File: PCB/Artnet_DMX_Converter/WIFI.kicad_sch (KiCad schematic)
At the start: 9 parts, among them J13 Conn_02x04

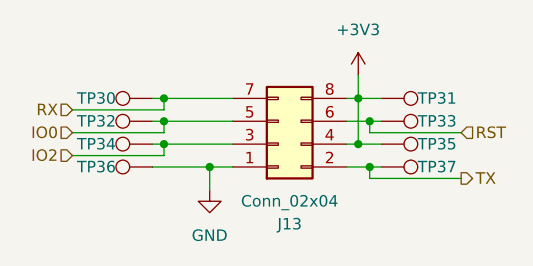
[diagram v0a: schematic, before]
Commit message: Testpoints and GND1 Fill
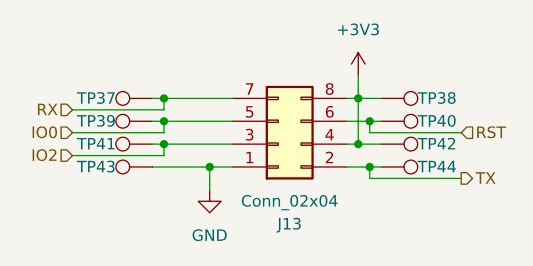
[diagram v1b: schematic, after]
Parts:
- renumbered TP30 to TP37, TP31 to TP38, TP32 to TP39, TP33 to TP40, TP34 to TP41, TP35 to TP42, TP36 to TP43, TP37 to TP44
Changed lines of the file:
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@@
 		(on_board yes)
 		(dnp no)
-		(property "Reference" "TP35"
+		(property "Reference" "TP42"
 			(at 155.194 87.63 90)
 			(effects
@@
 			(project "Artnet_DMX_Converter"
 				(path "/7d5b1976-98b3-4e47-ae52-3fe360235ea3/a6dafa22-90bf-43fa-b3bd-bb5c9d6a5370"
-					(reference "TP35")
+					(reference "TP42")
 					(unit 1)
 				)
@@
 		(dnp no)
 		(fields_autoplaced yes)
-		(property "Reference" "#PWR0135"
+		(property "Reference" "#PWR0140"
 			(at 148.59 83.82 0)
 			(effects
@@
 			(project ""
 				(path "/7d5b1976-98b3-4e47-ae52-3fe360235ea3/a6dafa22-90bf-43fa-b3bd-bb5c9d6a5370"
-					(reference "#PWR0135")
+					(reference "#PWR0140")
 					(unit 1)
 				)
@@
 		(on_board yes)
 		(dnp no)
-		(property "Reference" "TP30"
+		(property "Reference" "TP37"
 			(at 121.666 82.55 90)
 			(effects
@@
 			(project "Artnet_DMX_Converter"
 				(path "/7d5b1976-98b3-4e47-ae52-3fe360235ea3/a6dafa22-90bf-43fa-b3bd-bb5c9d6a5370"
-					(reference "TP30")
+					(reference "TP37")
 					(unit 1)
 				)
@@
 		(on_board yes)
 		(dnp no)
-		(property "Reference" "TP34"
+		(property "Reference" "TP41"
 			(at 121.666 87.63 90)
 			(effects
@@
 			(project "Artnet_DMX_Converter"
 				(path "/7d5b1976-98b3-4e47-ae52-3fe360235ea3/a6dafa22-90bf-43fa-b3bd-bb5c9d6a5370"
-					(reference "TP34")
+					(reference "TP41")
 					(unit 1)
 				)
@@
 		(dnp no)
 		(fields_autoplaced yes)
-		(property "Reference" "#PWR0136"
+		(property "Reference" "#PWR0141"
 			(at 132.08 99.06 0)
 			(effects
@@
 			(project ""
 				(path "/7d5b1976-98b3-4e47-ae52-3fe360235ea3/a6dafa22-90bf-43fa-b3bd-bb5c9d6a5370"
-					(reference "#PWR0136")
+					(reference "#PWR0141")
 					(unit 1)
 				)
@@
 		(on_board yes)
 		(dnp no)
-		(property "Reference" "TP36"
+		(property "Reference" "TP43"
 			(at 121.666 90.17 90)
 			(effects
@@
 			(project "Artnet_DMX_Converter"
 				(path "/7d5b1976-98b3-4e47-ae52-3fe360235ea3/a6dafa22-90bf-43fa-b3bd-bb5c9d6a5370"
-					(reference "TP36")
+					(reference "TP43")
 					(unit 1)
 				)
@@
 		(on_board yes)
 		(dnp no)
-		(property "Reference" "TP33"
+		(property "Reference" "TP40"
 			(at 155.194 85.09 90)
 			(effects
@@
 			(project "Artnet_DMX_Converter"
 				(path "/7d5b1976-98b3-4e47-ae52-3fe360235ea3/a6dafa22-90bf-43fa-b3bd-bb5c9d6a5370"
-					(reference "TP33")
+					(reference "TP40")
 					(unit 1)
 				)
@@
 		(on_board yes)
 		(dnp no)
-		(property "Reference" "TP32"
+		(property "Reference" "TP39"
 			(at 121.666 85.09 90)
 			(effects
@@
 			(project "Artnet_DMX_Converter"
 				(path "/7d5b1976-98b3-4e47-ae52-3fe360235ea3/a6dafa22-90bf-43fa-b3bd-bb5c9d6a5370"
-					(reference "TP32")
+					(reference "TP39")
 					(unit 1)
 				)
@@
 		(on_board yes)
 		(dnp no)
-		(property "Reference" "TP37"
+		(property "Reference" "TP44"
 			(at 155.194 90.17 90)
 			(effects
@@
 			(project "Artnet_DMX_Converter"
 				(path "/7d5b1976-98b3-4e47-ae52-3fe360235ea3/a6dafa22-90bf-43fa-b3bd-bb5c9d6a5370"
-					(reference "TP37")
+					(reference "TP44")
 					(unit 1)
 				)
@@
 		(on_board yes)
 		(dnp no)
-		(property "Reference" "TP31"
+		(property "Reference" "TP38"
 			(at 155.194 82.55 90)
 			(effects
@@
 			(project "Artnet_DMX_Converter"
 				(path "/7d5b1976-98b3-4e47-ae52-3fe360235ea3/a6dafa22-90bf-43fa-b3bd-bb5c9d6a5370"
-					(reference "TP31")
-					(unit 1)
-				)
+					(reference "TP38")
+					(unit 1)
+				)
